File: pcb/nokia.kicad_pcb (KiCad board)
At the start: 4 copper layers, 42.1 x 108 mm, 95 parts, among them J1 Conn_01x07, J2 USB_B_Micro, J20 Conn_01x04_Pin, J3 SM03B-SRSS-TB, J4 Conn_01x06_Pin, J6 SM03B-SRSS-TB, M1 Vibration, Q1 BC847, SW1 SW_Push, U1 W25Q128JVS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

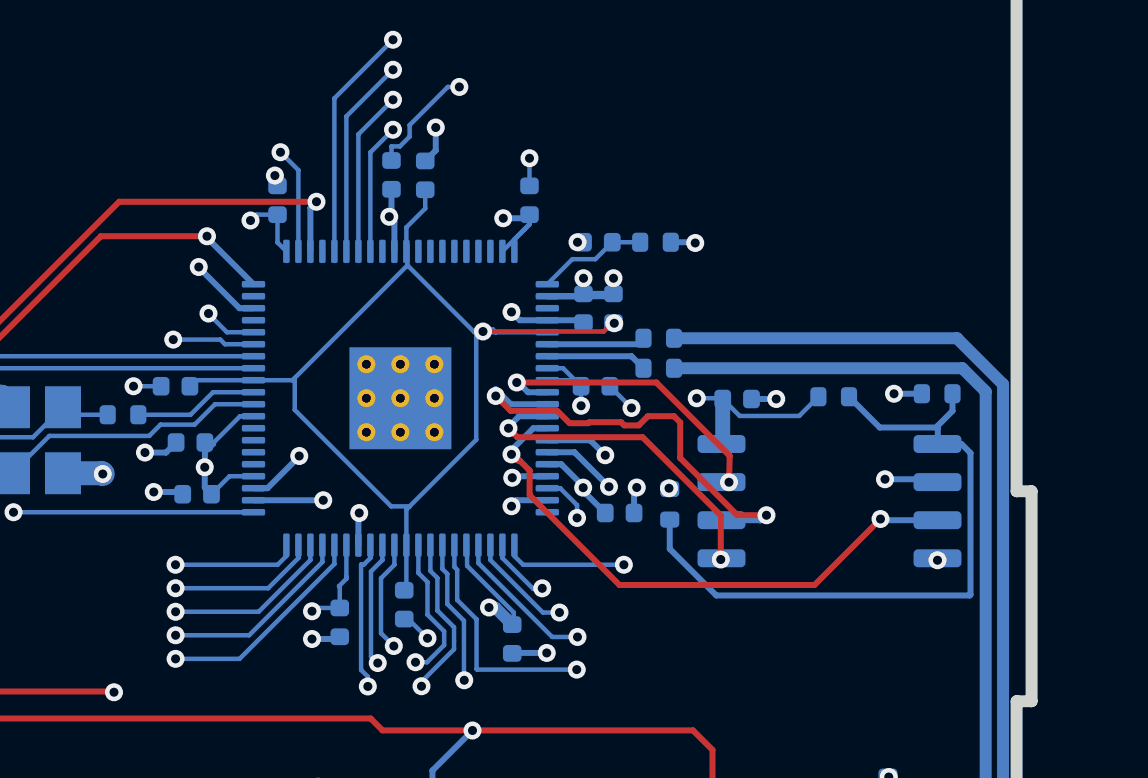
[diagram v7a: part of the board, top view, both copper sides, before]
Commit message: update renders, use zone for 1v1 net
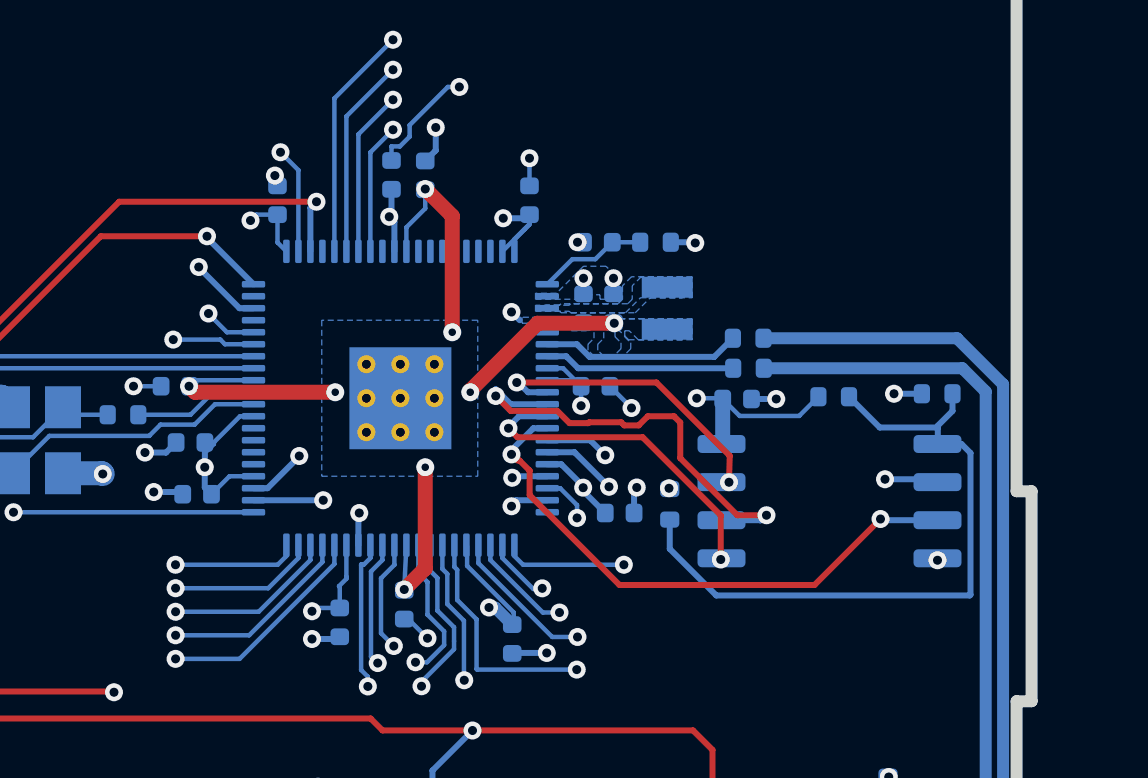
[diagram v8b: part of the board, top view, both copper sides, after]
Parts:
- added L1: 3.3u, RP2350_80QFN_minimal:L_pol_2016, B.Cu at (51.4, 57.2)
- moved R7 2.99 mm to (54.1, 59.2)
- moved R8 2.98 mm to (54.1, 58.2)
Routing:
- net +1V1: track 38.6 -> 26.5 mm, vias 2 -> 8
- net GND: track 56.7 -> 51.4 mm
- net Net-(U5-USB_DM): track 3.29 -> 6.62 mm
- net /USB_D+: track 84.1 -> 81.1 mm
- net Net-(U5-USB_DP): track 3.37 -> 6.36 mm
- net /USB_D-: track 85.1 -> 82.1 mm
- net +3V3: track 62.6 -> 60.5 mm
- added copper zone on B.Cu, net +1V1
- added copper zone on B.Cu, net +3V3
- added copper zone on B.Cu, net /VREG_LX
